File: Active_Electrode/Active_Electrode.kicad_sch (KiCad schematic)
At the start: 14 parts, among them J1 Conn_01x02, J2 Conn_01x09, U1 ADG442BNZ, U2 LF412CN

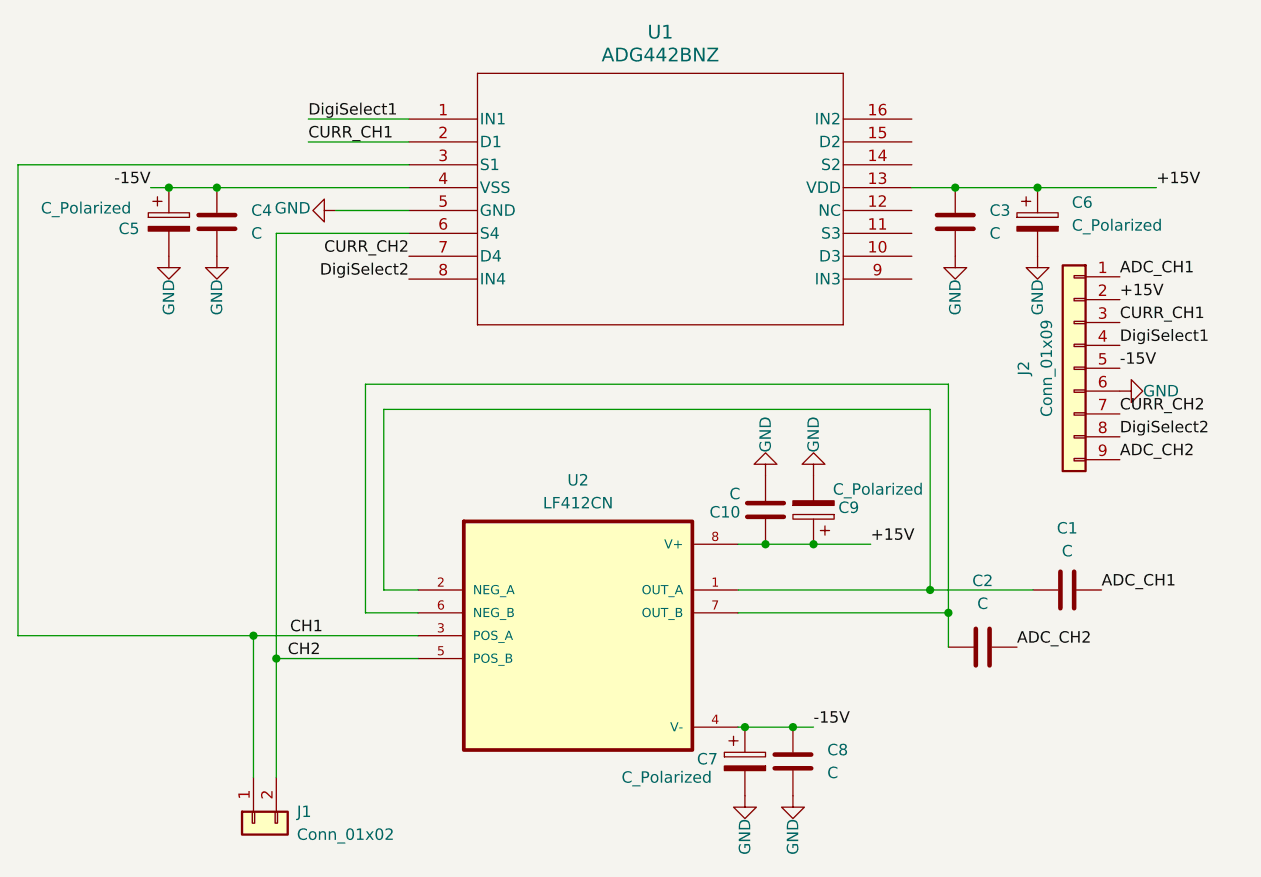
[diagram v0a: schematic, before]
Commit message: Modularize control script
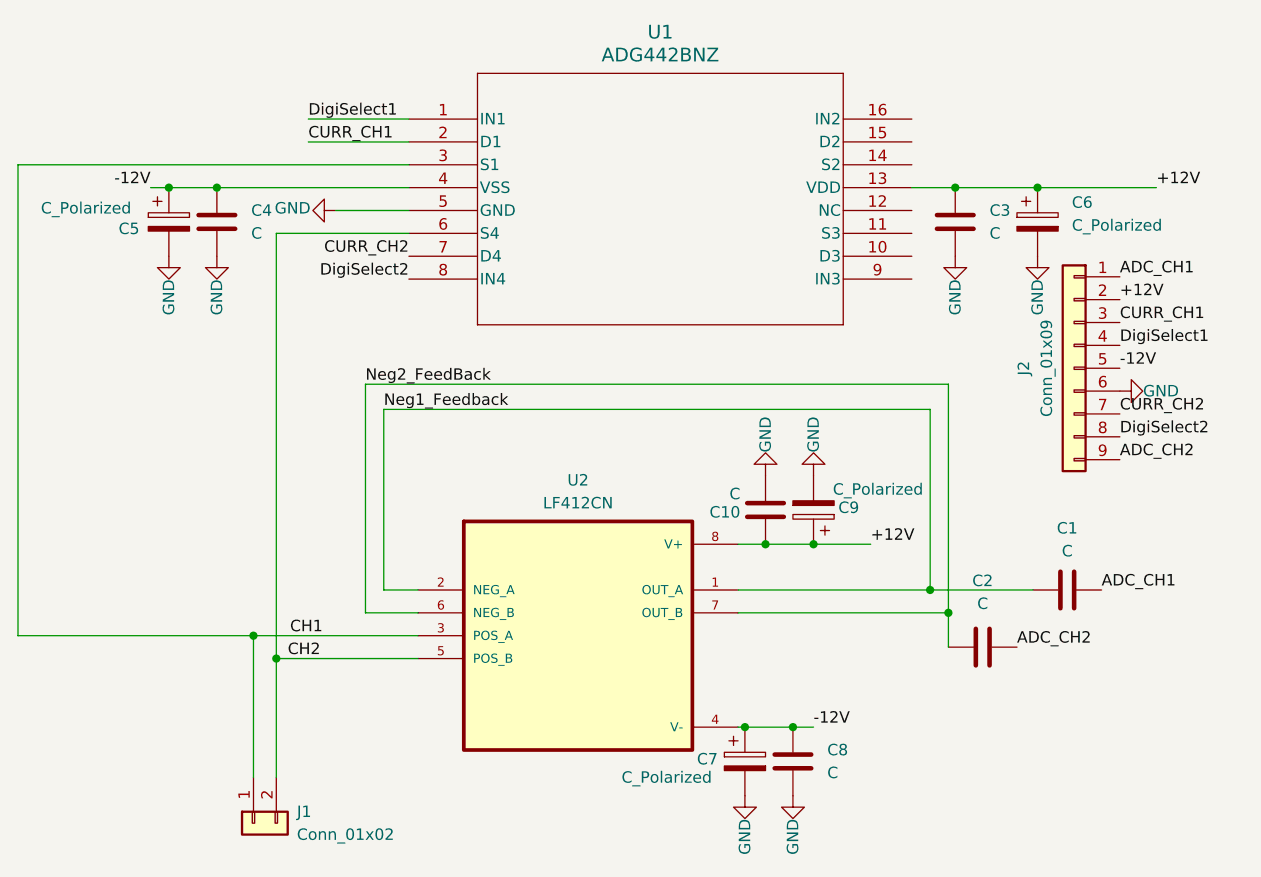
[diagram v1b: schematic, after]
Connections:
- net Neg1_Feedback: now reaches C1.1, U2.1 (OUT_A), U2.2 (NEG_A)
- net Neg2_FeedBack: now reaches C2.1, U2.6 (NEG_B), U2.7 (OUT_B)
- net +15V renamed +12V
- net -15V renamed -12V
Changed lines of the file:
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@@
     (effects (font (size 1.27 1.27)) (justify right bottom))
   )
-  (label "+15V" (at 129.032 106.172 0) (fields_autoplaced)
+  (label "Neg1_Feedback" (at 74.93 91.186 0) (fields_autoplaced)
     (effects (font (size 1.27 1.27)) (justify left bottom))
   )
-  (label "-15V" (at 49.022 66.548 180) (fields_autoplaced)
+  (label "+12V" (at 129.032 106.172 0) (fields_autoplaced)
+    (effects (font (size 1.27 1.27)) (justify left bottom))
+  )
+  (label "-12V" (at 49.022 66.548 180) (fields_autoplaced)
     (effects (font (size 1.27 1.27)) (justify right bottom))
   )
@@
     (effects (font (size 1.27 1.27)) (justify left bottom))
   )
-  (label "-15V" (at 156.718 86.614 0) (fields_autoplaced)
+  (label "-12V" (at 156.718 86.614 0) (fields_autoplaced)
     (effects (font (size 1.27 1.27)) (justify left bottom))
   )
-  (label "+15V" (at 156.718 78.994 0) (fields_autoplaced)
+  (label "+12V" (at 156.718 78.994 0) (fields_autoplaced)
+    (effects (font (size 1.27 1.27)) (justify left bottom))
+  )
+  (label "Neg2_FeedBack" (at 72.898 88.392 0) (fields_autoplaced)
     (effects (font (size 1.27 1.27)) (justify left bottom))
   )
@@
     (effects (font (size 1.27 1.27)) (justify left bottom))
   )
-  (label "+15V" (at 160.782 66.548 0) (fields_autoplaced)
+  (label "+12V" (at 160.782 66.548 0) (fields_autoplaced)
     (effects (font (size 1.27 1.27)) (justify left bottom))
   )
-  (label "-15V" (at 122.682 126.492 0) (fields_autoplaced)
+  (label "-12V" (at 122.682 126.492 0) (fields_autoplaced)
     (effects (font (size 1.27 1.27)) (justify left bottom))
   )

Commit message: Corrections made to active electrode and made 2 more
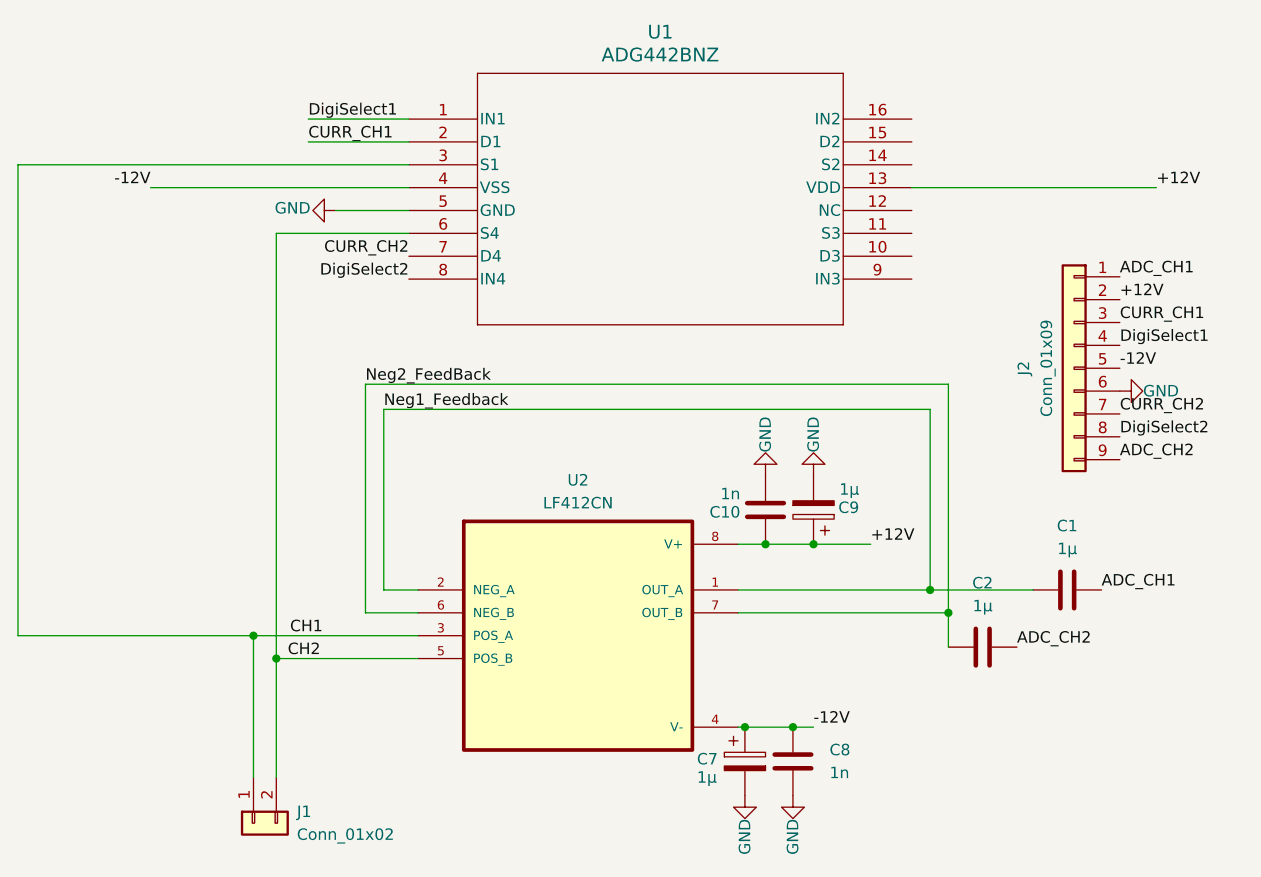
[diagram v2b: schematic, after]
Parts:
- removed C3, C4: C, Capacitor_THT:C_Disc_D4.3mm_W1.9mm_P5.00mm, symbol Device:C
- removed C5, C6: C_Polarized, Capacitor_THT:C_Disc_D4.3mm_W1.9mm_P5.00mm, symbol Device:C_Polarized
- C1, C2: value C -> 1µ
- C10, C8: value C -> 1n
- C7, C9: value C_Polarized -> 1µ

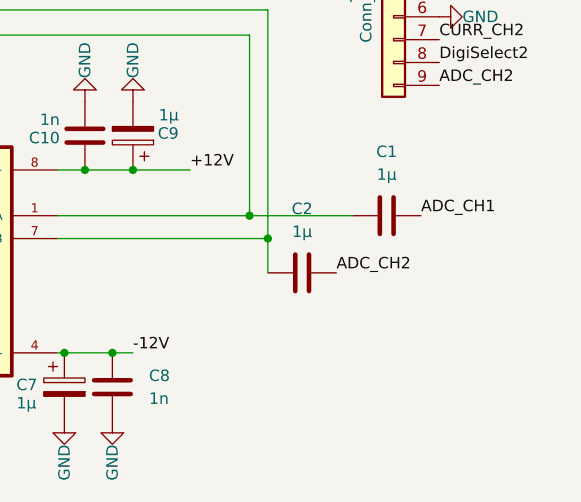
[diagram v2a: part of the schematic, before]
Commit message: Updated active electrode and other boards
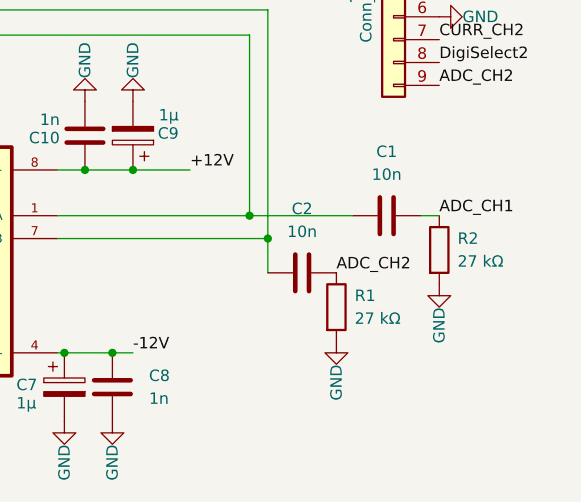
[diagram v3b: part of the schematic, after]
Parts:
- added R1, R2: 27 kΩ, Resistor_THT:R_Axial_DIN0207_L6.3mm_D2.5mm_P7.62mm_Horizontal, symbol Device:R
- C1, C2: value 1µ -> 10n
- C7, C9: footprint Capacitor_THT:C_Disc_D4.3mm_W1.9mm_P5.00mm -> Capacitor_THT:CP_Radial_Tantal_D5.5mm_P5.00mm
- C8: footprint Capacitor_THT:C_Disc_D4.3mm_W1.9mm_P5.00mm -> Capacitor_THT:C_Disc_D6.0mm_W2.5mm_P5.00mm
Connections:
- net ADC_CH1: now also R2.1
- net ADC_CH2: now also R1.1
- net GND: now also R1.2, R2.2
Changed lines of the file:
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@@
+    (stroke (width 0) (type default))
+  )
+  (wire (pts (xy 156.718 111.252) (xy 154.686 111.252))
     (stroke (width 0) (type default))
   )
@@
   (wire (pts (xy 34.29 116.332) (xy 60.452 116.332))
     (stroke (width 0) (type default))
-  )
-  (label "ADC_CH2" (at 145.288 117.602 0) (fields_autoplaced)
-    (effects (font (size 1.27 1.27)) (justify left bottom))
-  )
-  (label "ADC_CH1" (at 154.686 111.252 0) (fields_autoplaced)
-    (effects (font (size 1.27 1.27)) (justify left bottom))
   )
   (label "CH1" (at 64.516 116.332 0) (fields_autoplaced)
@@
     (effects (font (size 1.27 1.27)) (justify right bottom))
   )
+  (label "ADC_CH1" (at 156.718 111.252 0) (fields_autoplaced)
+    (effects (font (size 1.27 1.27)) (justify left bottom))
+  )
+  (label "ADC_CH2" (at 145.288 117.602 0) (fields_autoplaced)
+    (effects (font (size 1.27 1.27)) (justify left bottom))
+  )
   (label "ADC_CH2" (at 156.718 96.774 0) (fields_autoplaced)
     (effects (font (size 1.27 1.27)) (justify left bottom))
@@
       (effects (font (size 1.27 1.27)) (justify left))
     )
-    (property "Footprint" "Capacitor_THT:C_Disc_D4.3mm_W1.9mm_P5.00mm" (at 121.7168 98.552 0)
+    (property "Footprint" "Capacitor_THT:CP_Radial_Tantal_D5.5mm_P5.00mm" (at 121.7168 98.552 0)
       (effects (font (size 1.27 1.27)) hide)
     )
@@
       (effects (font (size 1.27 1.27)) (justify left))
     )
-    (property "Footprint" "Capacitor_THT:C_Disc_D4.3mm_W1.9mm_P5.00mm" (at 121.3612 134.112 0)
+    (property "Footprint" "Capacitor_THT:C_Disc_D6.0mm_W2.5mm_P5.00mm" (at 121.3612 134.112 0)
       (effects (font (size 1.27 1.27)) hide)
     )
@@
         (path "/4027ca50-1451-47b5-ae34-bbaf8d3c8745"
           (reference "C8") (unit 1)
+        )
+      )
+    )
+  )
+  (symbol (lib_id "power:GND") (at 145.288 125.222 0) (mirror y) (unit 1)
+    (in_bom yes) (on_board yes) (dnp no)
+    (property "Reference" "#PWR03" (at 145.288 131.572 0)
+      (effects (font (size 1.27 1.27)) hide)
+    )
+    (property "Value" "GND" (at 145.288 129.794 90)
+      (effects (font (size 1.27 1.27)))
+    )
+    (property "Footprint" "" (at 145.288 125.222 0)
+      (effects (font (size 1.27 1.27)) hide)
+    )
+    (property "Datasheet" "" (at 145.288 125.222 0)
+      (effects (font (size 1.27 1.27)) hide)
+    )
+    (pin "1")
+    (instances
+      (project "Active_Electrode"
+        (path "/4027ca50-1451-47b5-ae34-bbaf8d3c8745"
+          (reference "#PWR03") (unit 1)
         )
       )
@@
       (effects (font (size 1.27 1.27)) (justify left))
     )
-    (property "Footprint" "Capacitor_THT:C_Disc_D4.3mm_W1.9mm_P5.00mm" (at 116.0272 134.112 0)
+    (property "Footprint" "Capacitor_THT:CP_Radial_Tantal_D5.5mm_P5.00mm" (at 116.0272 134.112 0)
       (effects (font (size 1.27 1.27)) hide)
     )
@@
     )
   )
+  (symbol (lib_id "Device:R") (at 156.718 115.062 0) (unit 1)
+    (in_bom yes) (on_board yes) (dnp no) (fields_autoplaced)
+    (property "Reference" "R2" (at 158.75 113.792 0)
+      (effects (font (size 1.27 1.27)) (justify left))
+    )
+    (property "Value" "27 kΩ" (at 158.75 116.332 0)
+      (effects (font (size 1.27 1.27)) (justify left))
+    )
+    (property "Footprint" "Resistor_THT:R_Axial_DIN0207_L6.3mm_D2.5mm_P7.62mm_Horizontal" (at 154.94 115.062 90)
+      (effects (font (size 1.27 1.27)) hide)
+    )
+    (property "Datasheet" "~" (at 156.718 115.062 0)
+      (effects (font (size 1.27 1.27)) hide)
+    )
+    (pin "2")
+    (pin "1")
+    (instances
+      (project "Active_Electrode"
+        (path "/4027ca50-1451-47b5-ae34-bbaf8d3c8745"
+          (reference "R2") (unit 1)
+        )
+      )
+    )
+  )
   (symbol (lib_id "power:GND") (at 156.718 89.154 90) (mirror x) (unit 1)
     (in_bom yes) (on_board yes) (dnp no)
@@
       (effects (font (size 1.27 1.27)))
     )
-    (property "Value" "1µ" (at 150.876 106.68 90)
+    (property "Value" "10n" (at 150.876 106.68 90)
       (effects (font (size 1.27 1.27)))
     )
@@
       (effects (font (size 1.27 1.27)))
     )
-    (property "Value" "1µ" (at 141.478 113.03 90)
+    (property "Value" "10n" (at 141.478 113.03 90)
       (effects (font (size 1.27 1.27)))
     )
@@
     )
   )
+  (symbol (lib_id "power:GND") (at 156.718 118.872 0) (mirror y) (unit 1)
+    (in_bom yes) (on_board yes) (dnp no)
+    (property "Reference" "#PWR04" (at 156.718 125.222 0)
+      (effects (font (size 1.27 1.27)) hide)
+    )
+    (property "Value" "GND" (at 156.718 123.444 90)
+      (effects (font (size 1.27 1.27)))
+    )
+    (property "Footprint" "" (at 156.718 118.872 0)
+      (effects (font (size 1.27 1.27)) hide)
+    )
+    (property "Datasheet" "" (at 156.718 118.872 0)
+      (effects (font (size 1.27 1.27)) hide)
+    )
+    (pin "1")
+    (instances
+      (project "Active_Electrode"
+        (path "/4027ca50-1451-47b5-ae34-bbaf8d3c8745"
+          (reference "#PWR04") (unit 1)
+        )
+      )
+    )
+  )
   (symbol (lib_id "power:GND") (at 122.682 98.552 0) (mirror x) (unit 1)
     (in_bom yes) (on_board yes) (dnp no)
@@
         )
       )
+    )
+  )
+  (symbol (lib_id "Device:R") (at 145.288 121.412 0) (unit 1)
+    (in_bom yes) (on_board yes) (dnp no) (fields_autoplaced)
+    (property "Reference" "R1" (at 147.32 120.142 0)
+      (effects (font (size 1.27 1.27)) (justify left))
+    )
+    (property "Value" "27 kΩ" (at 147.32 122.682 0)
+      (effects (font (size 1.27 1.27)) (justify left))
+    )
+    (property "Footprint" "Resistor_THT:R_Axial_DIN0207_L6.3mm_D2.5mm_P7.62mm_Horizontal" (at 143.51 121.412 90)
+      (effects (font (size 1.27 1.27)) hide)
+    )
+    (property "Datasheet" "~" (at 145.288 121.412 0)
+      (effects (font (size 1.27 1.27)) hide)
+    )
+    (pin "1")
+    (pin "2")
+    (instances
+      (project "Active_Electrode"
+        (path "/4027ca50-1451-47b5-ae34-bbaf8d3c8745"
+          (reference "R1") (unit 1)
+        )
+      )
